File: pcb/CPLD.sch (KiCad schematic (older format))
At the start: 2 parts

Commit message: Removed the POW multiplexer lines and put the standard interrupt lines
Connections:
- net labels removed: DEN_GYR, POW_MULT2
- wire segments 95 -> 93
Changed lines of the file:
@@
-EESchema Schematic File Version 2  date 12/12/2012 5:26:02 PM
+EESchema Schematic File Version 2  date 12/16/2012 4:31:25 PM
 LIBS:power
 LIBS:device
@@
 $Descr A4 11700 8267
 encoding utf-8
-Sheet 2 10
+Sheet 2 9
 Title ""
-Date "12 dec 2012"
+Date "16 dec 2012"
 Rev ""
 Comp ""
@@
 	9600 5450 9300 5450
 Wire Wire Line
-	1950 5600 2200 5600
-Wire Wire Line
 	1950 5300 2200 5300
 Wire Wire Line
@@
 Wire Wire Line
 	9600 4000 9300 4000
-Wire Wire Line
-	9600 3600 9300 3600
 Wire Wire Line
 	9600 3400 9300 3400
@@
 	1    0    0    -1
 $EndComp
-Text Label 7000 4200 0    60   ~ 0
-POW_MULT2
 Text Label 7000 4300 0    60   ~ 0
 POW_MULT1
@@
 Text HLabel 1950 5450 0    60   Input ~ 0
 POW_MULT1
-Text HLabel 1950 5600 0    60   Input ~ 0
-POW_MULT2
 Text Label 2200 5300 0    60   ~ 0
 POW_MULT0
 Text Label 2200 5450 0    60   ~ 0
 POW_MULT1
-Text Label 2200 5600 0    60   ~ 0
-POW_MULT2
 Text Label 5350 2450 1    60   ~ 0
 nCS
@@
 Text Label 5650 5000 3    60   ~ 0
 RF_IRQ
-Text Label 7000 4100 0    60   ~ 0
-DEN_GYR
 Text Label 7000 4000 0    60   ~ 0
 INT2_GYR
@@
 Text Label 9300 4000 2    60   ~ 0
 RF_IRQ
-Text Label 9300 3600 2    60   ~ 0
-DEN_GYR
 Text Label 9300 3500 2    60   ~ 0
 INT2_GYR
@@
 Text HLabel 9600 4000 2    60   Input ~ 0
 RF_IRQ
-Text HLabel 9600 3600 2    60   Input ~ 0
-DEN_GYR
 Text HLabel 9600 3500 2    60   Input ~ 0
 INT2_GYR/DRDY

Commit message: CPLD connection finished.
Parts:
- added S? (x4): EVQ-Q2S03W, symbol EVQ-Q2S03W
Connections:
- net labels added: EXTI11, EXTI12, EXTI13, EXTI15, S1, S2, S3, S4
- net labels removed: EXTI9, POW_9V, POW_MULT0, POW_MULT1
- wire segments 93 -> 112
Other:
- note added: "Suggested Interrupt Setup:\nIndependent Vectors:\n EXTI0: LIS302_INT1\n EXTI1: LIS302_INT2\n EXTI2: SPI_IRQ_RF\n EXTI3: SPI_IRQ_TOUCH\n EXTI4:\n\nEXTI9_5:\n EXTI5: S1\n EXTI6: S2\n EXTI7: S3\n EXTI8: S4\n EXTI9:\n\nEXTI15_10:\n EXTI10: \n EXTI11: INT1_A\n EXTI12: INT1_G\n EXTI13: INT2_A\n EXTI14: \n EXTI15: DRDYg/INT2_G"

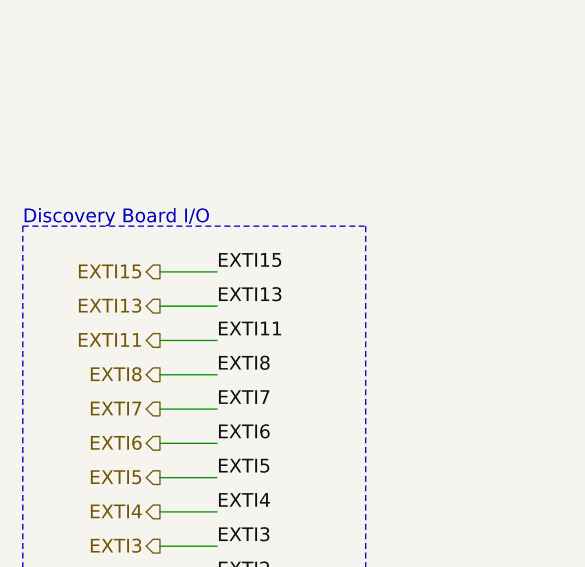
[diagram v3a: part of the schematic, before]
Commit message: Switched the interrupt line location so that we can use one of the ADC channels for the audio.
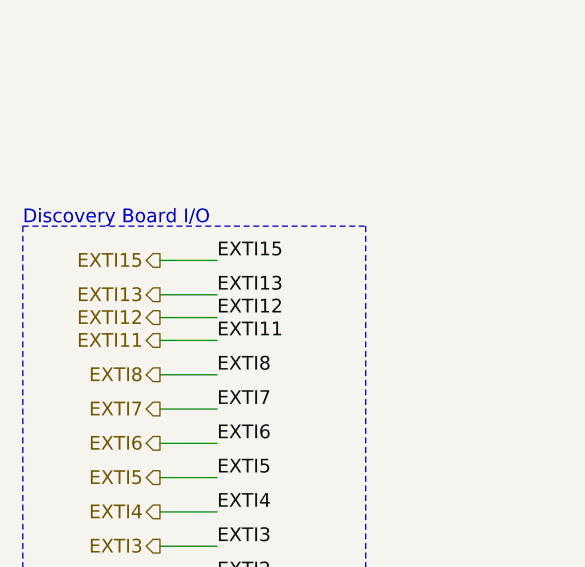
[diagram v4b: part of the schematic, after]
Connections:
- wire segments 112 -> 113
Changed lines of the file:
@@
-EESchema Schematic File Version 2  date 12/19/2012 4:02:29 PM
+EESchema Schematic File Version 2  date 12/19/2012 4:17:57 PM
 LIBS:power
 LIBS:device
@@
 Comment4 ""
 $EndDescr
+Wire Wire Line
+	1900 3400 2150 3400
+Text Label 2150 3400 0    60   ~ 0
+EXTI12
+Text HLabel 1900 3400 0    60   Output ~ 0
+EXTI12
 Text Label 7350 2800 0    60   ~ 0
 EXTI15
 Wire Wire Line
-	1900 3200 2150 3200
-Text Label 2150 3200 0    60   ~ 0
+	1900 3150 2150 3150
+Text Label 2150 3150 0    60   ~ 0
 EXTI15
-Text HLabel 1900 3200 0    60   Output ~ 0
+Text HLabel 1900 3150 0    60   Output ~ 0
 EXTI15
 Text HLabel 1900 3500 0    60   Output ~ 0
 EXTI11
-Text HLabel 1900 3350 0    60   Output ~ 0
+Text HLabel 1900 3300 0    60   Output ~ 0
 EXTI13
-Text Label 2150 3350 0    60   ~ 0
+Text Label 2150 3300 0    60   ~ 0
 EXTI13
 Text Label 2150 3500 0    60   ~ 0
@@
 	1900 3500 2150 3500
 Wire Wire Line
-	1900 3350 2150 3350
+	1900 3300 2150 3300
 Text Label 4750 3000 2    60   ~ 0
 EXTI13
